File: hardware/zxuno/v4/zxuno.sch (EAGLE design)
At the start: 103 parts, among them T1 BC846, U1 6SLX9TQG144, U2 FLASH-SPI-25XXSMD1, U4 AD724, U5 50MHz, U6 3.3V, U7 1.2V, Y1 3.58M, Y2 4.43M

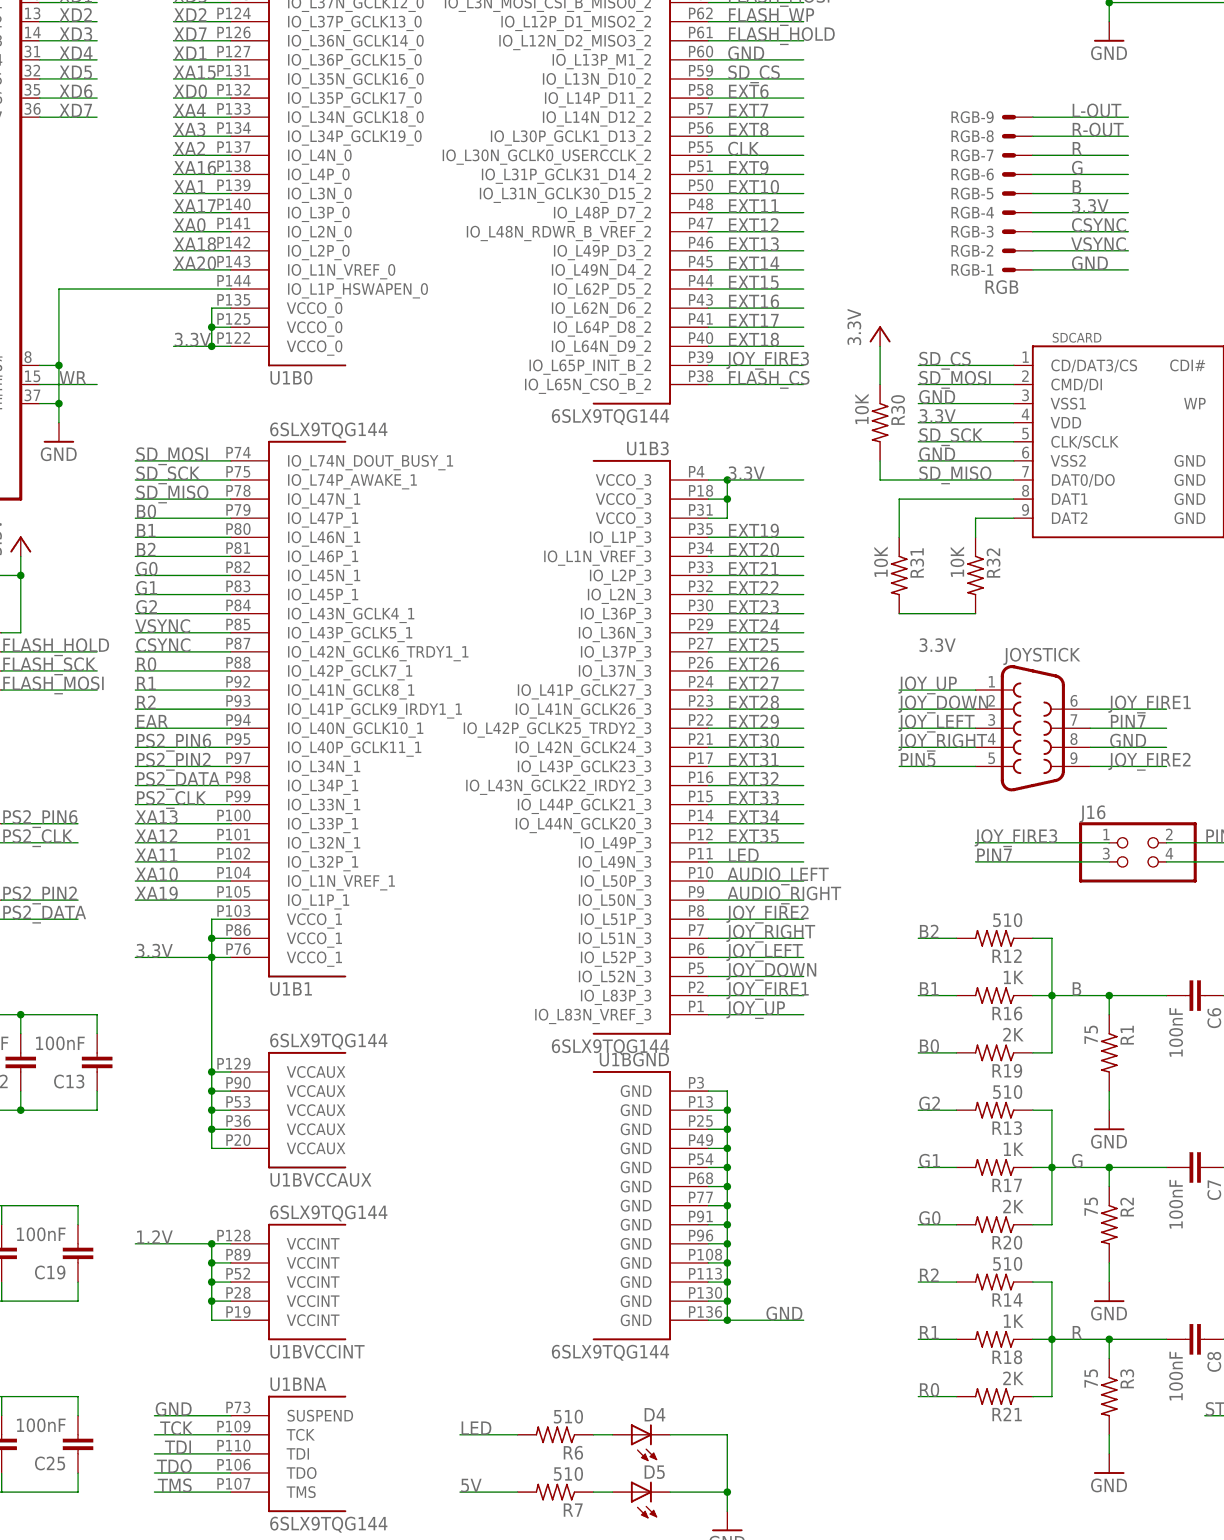
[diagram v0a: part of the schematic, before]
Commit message: Cambio nomeclatura pines B y R para que coincida con v4.1
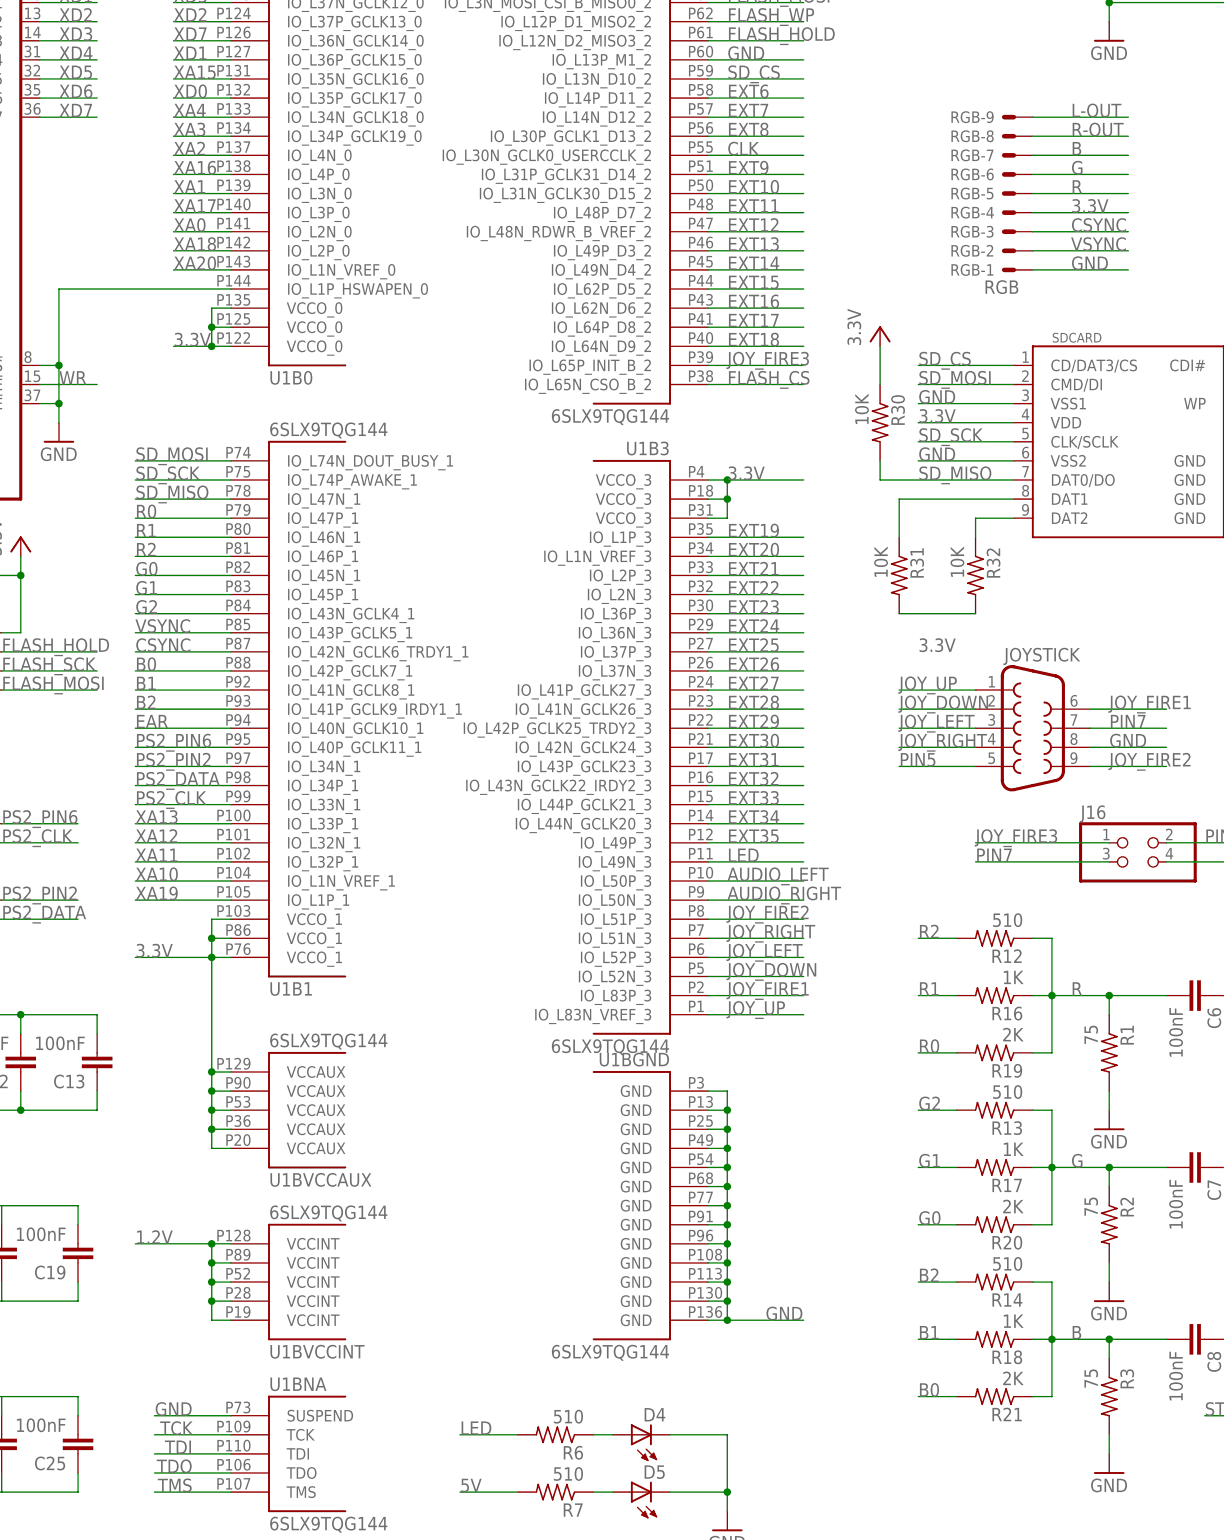
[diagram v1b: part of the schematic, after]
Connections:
- net B: now also C8.2, R14.1, R18.1, R21.1, R3.1, RGB-7.S; no longer C6.2, R1.1, R12.1, R16.1, R19.1, RGB-5.S
- net B0: now also R21.2, U1B1.IO_L42P_GCLK7_1; no longer R19.2, U1B1.IO_L47P_1
- net B1: now also R18.2, U1B1.IO_L41N_GCLK8_1; no longer R16.2, U1B1.IO_L46N_1
- net B2: now also R14.2, U1B1.IO_L41P_GCLK9_IRDY1_1; no longer R12.2, U1B1.IO_L46P_1
- net R: now also C6.2, R1.1, R12.1, R16.1, R19.1, RGB-5.S; no longer C8.2, R14.1, R18.1, R21.1, R3.1, RGB-7.S
- net R0: now also R19.2, U1B1.IO_L47P_1; no longer R21.2, U1B1.IO_L42P_GCLK7_1
- net R1: now also R16.2, U1B1.IO_L46N_1; no longer R18.2, U1B1.IO_L41N_GCLK8_1
- net R2: now also R12.2, U1B1.IO_L46P_1; no longer R14.2, U1B1.IO_L41P_GCLK9_IRDY1_1
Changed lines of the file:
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@@
 <?xml version="1.0" encoding="utf-8"?>
 <!DOCTYPE eagle SYSTEM "eagle.dtd">
-<eagle version="6.5.0">
+<eagle version="7.3.0">
 <drawing>
 <settings>
@@
 </segment>
 </net>
-<net name="B0" class="0">
+<net name="R0" class="0">
 <segment>
 <wire x1="35.56" y1="-7.62" x2="22.86" y2="-7.62" width="0.1524" layer="91"/>
@@
 </segment>
 </net>
-<net name="B1" class="0">
+<net name="R1" class="0">
 <segment>
 <wire x1="35.56" y1="-10.16" x2="22.86" y2="-10.16" width="0.1524" layer="91"/>
@@
 </segment>
 </net>
-<net name="B2" class="0">
+<net name="R2" class="0">
 <segment>
 <wire x1="35.56" y1="-12.7" x2="22.86" y2="-12.7" width="0.1524" layer="91"/>
@@
 </segment>
 </net>
-<net name="R0" class="0">
+<net name="B0" class="0">
 <segment>
 <wire x1="35.56" y1="-27.94" x2="22.86" y2="-27.94" width="0.1524" layer="91"/>
@@
 </segment>
 </net>
-<net name="R1" class="0">
+<net name="B1" class="0">
 <segment>
 <wire x1="35.56" y1="-30.48" x2="22.86" y2="-30.48" width="0.1524" layer="91"/>
@@
 </segment>
 </net>
-<net name="R2" class="0">
+<net name="B2" class="0">
 <segment>
 <wire x1="35.56" y1="-33.02" x2="22.86" y2="-33.02" width="0.1524" layer="91"/>
@@
 </segment>
 </net>
-<net name="B" class="0">
+<net name="R" class="0">
 <segment>
 <wire x1="154.94" y1="35.56" x2="142.24" y2="35.56" width="0.1524" layer="91"/>
@@
 </segment>
 </net>
-<net name="R" class="0">
+<net name="B" class="0">
 <segment>
 <pinref part="R14" gate="G$1" pin="1"/>
